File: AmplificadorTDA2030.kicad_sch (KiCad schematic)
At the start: 36 parts, among them J1 SJ1-3523N, J2 DC-005, J3 Speaker, U1 TDA2030, U2 TDA2030

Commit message: Librerias de Simbolos,Footprints y Modelos 3D Agregados
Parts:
- J2: footprint Footprints y Simbolos:NINIGI_DC-005 -> DC-005 - Connector Alimentacion:NINIGI_DC-005
- RV1: footprint Connector_PinSocket_2.00mm:PinSocket_2x03_P2.00mm_Vertical -> Potentiometer_THT:Potentiometer_Alps_RK163_Dual_Horizontal
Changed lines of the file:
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@@
 			)
 		)
-		(property "Footprint" "Connector_PinSocket_2.00mm:PinSocket_2x03_P2.00mm_Vertical"
+		(property "Footprint" "Potentiometer_THT:Potentiometer_Alps_RK163_Dual_Horizontal"
 			(at 118.745 86.36 0)
 			(effects
@@
 			)
 		)
-		(property "Footprint" "Footprints y Simbolos:NINIGI_DC-005"
+		(property "Footprint" "DC-005 - Connector Alimentacion:NINIGI_DC-005"
 			(at 91.44 38.1 0)
 			(effects

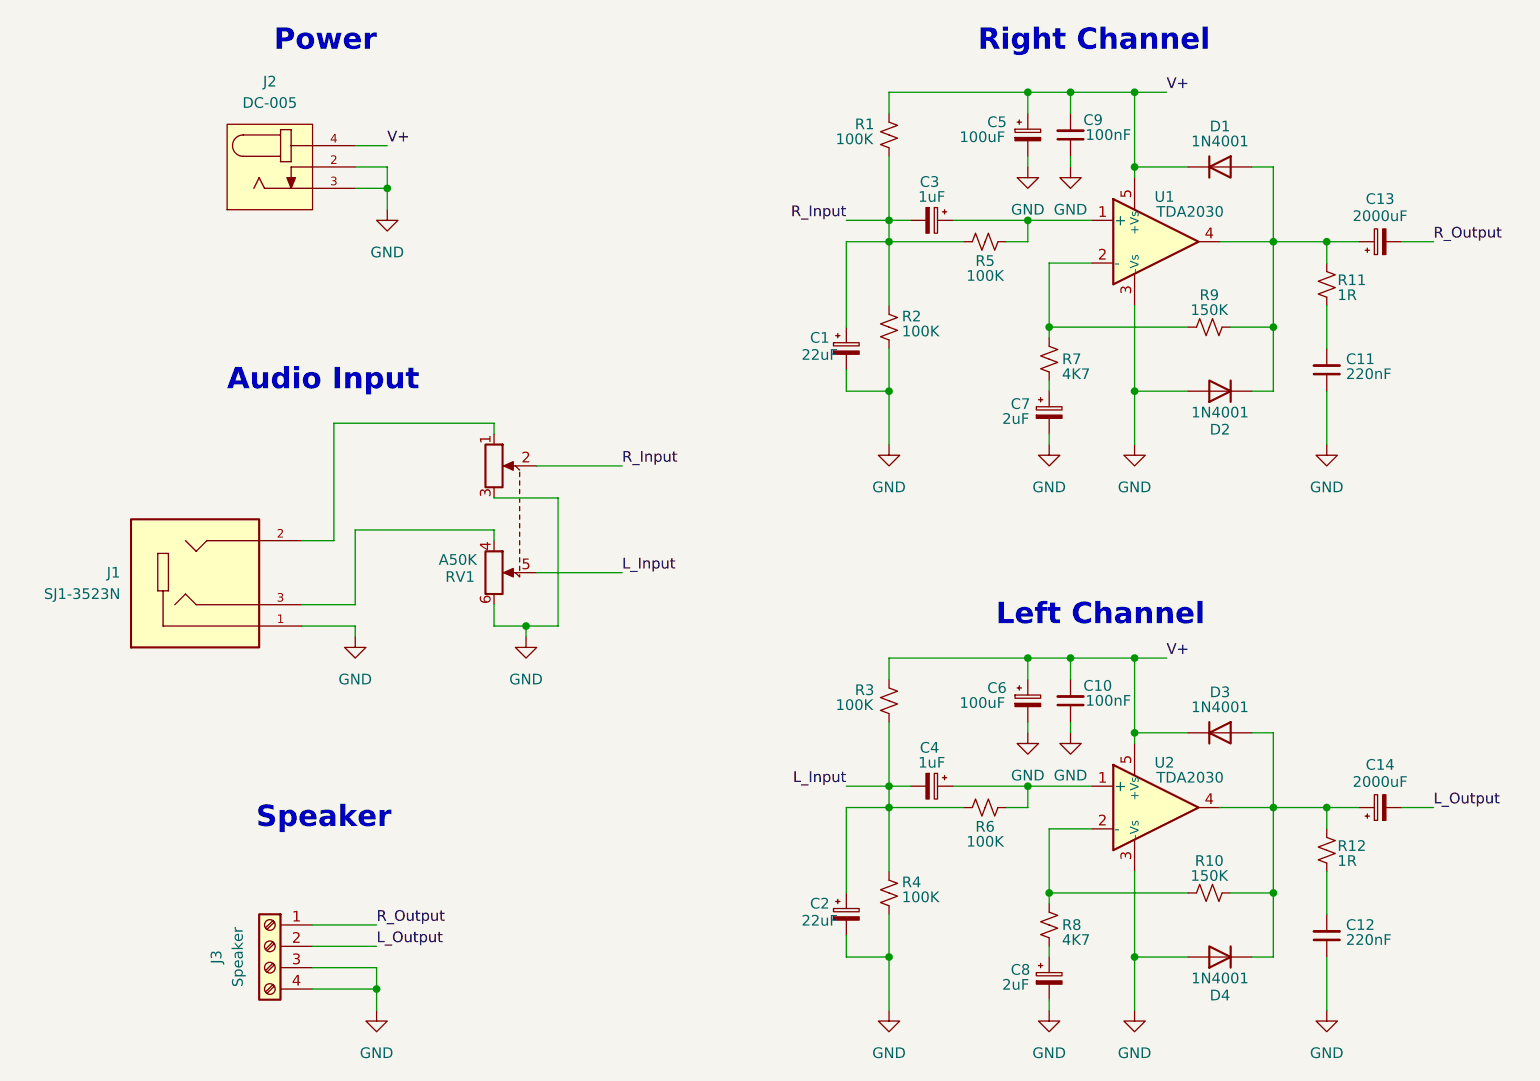
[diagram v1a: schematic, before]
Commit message: Footprints Asignados
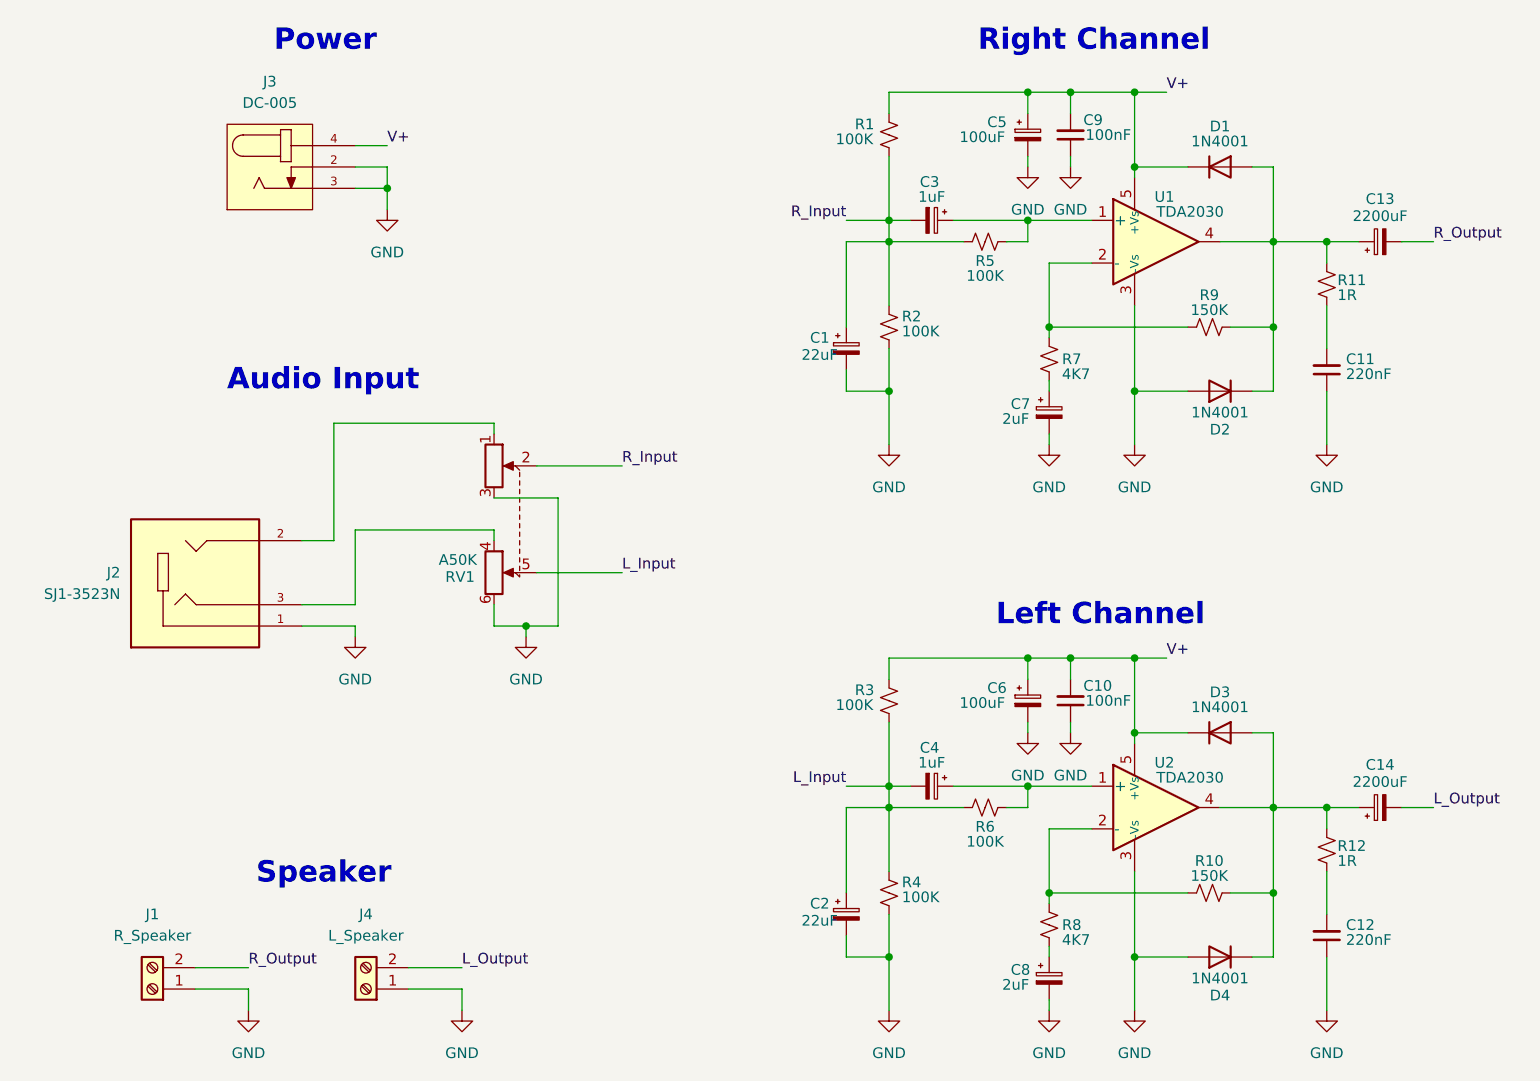
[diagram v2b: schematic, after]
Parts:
- removed J3: Speaker, Connector:FanPinHeader_1x04_P2.54mm_Vertical, symbol Connector:Screw_Terminal_01x04
- added J1: R_Speaker, TerminalBlock_Phoenix:TerminalBlock_Phoenix_MKDS-1,5-2-5.08_1x02_P5.08mm_Horizontal, symbol Connector:Screw_Terminal_01x02
- added J4: L_Speaker, TerminalBlock_Phoenix:TerminalBlock_Phoenix_MKDS-1,5-2-5.08_1x02_P5.08mm_Horizontal, symbol Connector:Screw_Terminal_01x02
- C1, C2, C5, C6: footprint Capacitor_THT:CP_Radial_D10.0mm_P5.00mm -> Capacitor_THT:CP_Radial_D6.3mm_P2.50mm
- C10, C11, C12, C9: footprint Capacitor_THT:CP_Radial_D10.0mm_P5.00mm -> Capacitor_THT:C_Disc_D3.0mm_W2.0mm_P2.50mm
- C13, C14: value 2000uF -> 2200uF; footprint Capacitor_THT:CP_Radial_D10.0mm_P5.00mm -> Capacitor_THT:CP_Radial_D16.0mm_P7.50mm
- C3, C4, C7, C8: footprint Capacitor_THT:CP_Radial_D10.0mm_P5.00mm -> Capacitor_THT:CP_Radial_D4.0mm_P2.00mm
- renumbered J1 to J2, J2 to J3
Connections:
- net GND: now also J1.1 (Pin_1), J4.1 (Pin_1)
- net L_Output: now also J4.2 (Pin_2)
- net R_Output: now also J1.2 (Pin_2)

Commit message: Ruteo de PCB correcto
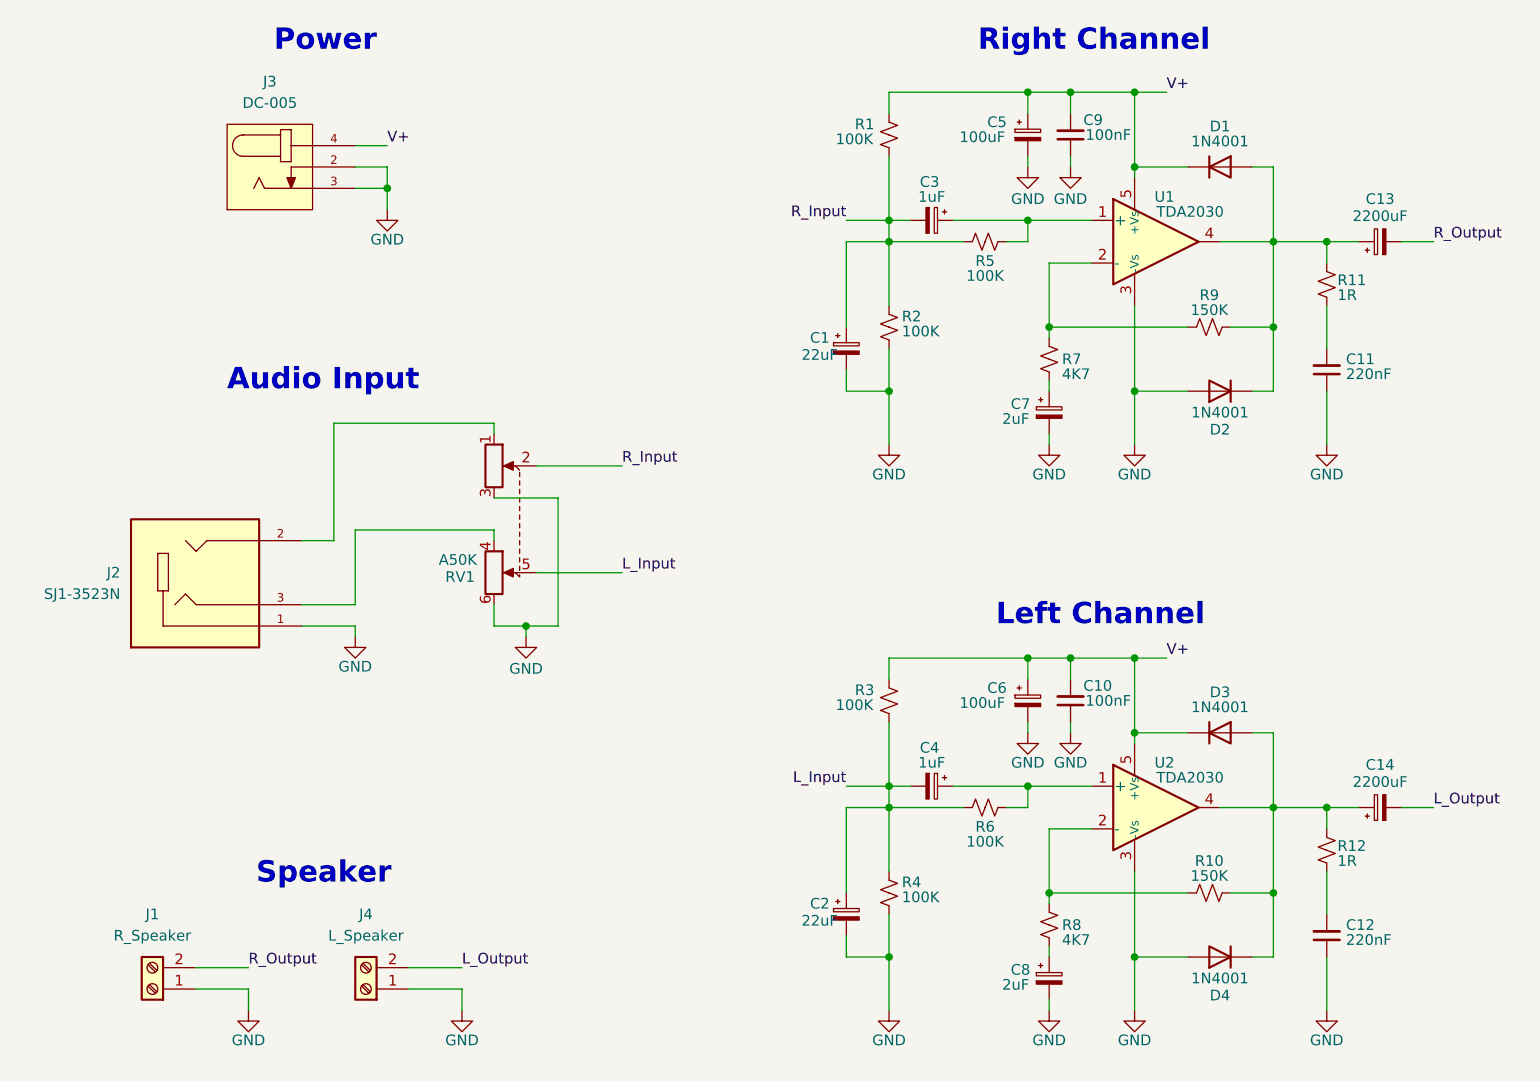
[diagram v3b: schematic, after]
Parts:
- R10, R11, R12, R7, R9: footprint Resistor_THT:R_Axial_DIN0204_L3.6mm_D1.6mm_P5.08mm_Horizontal -> Resistor_THT:R_Axial_DIN0204_L3.6mm_D1.6mm_P7.62mm_Horizontal
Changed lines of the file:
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@@
 			)
 		)
-		(property "Footprint" "Resistor_THT:R_Axial_DIN0204_L3.6mm_D1.6mm_P5.08mm_Horizontal"
+		(property "Footprint" "Resistor_THT:R_Axial_DIN0204_L3.6mm_D1.6mm_P7.62mm_Horizontal"
 			(at 203.2 57.15 0)
 			(effects
@@
 		(on_board yes)
 		(dnp no)
-		(fields_autoplaced yes)
 		(property "Reference" "#PWR06"
 			(at 165.1 77.47 0)
@@
 		)
 		(property "Value" "GND"
-			(at 165.1 76.2 0)
+			(at 165.1 74.676 0)
 			(effects
 				(font
@@
 		(on_board yes)
 		(dnp no)
-		(fields_autoplaced yes)
 		(property "Reference" "#PWR010"
 			(at 184.15 77.47 0)
@@
 		)
 		(property "Value" "GND"
-			(at 184.15 76.2 0)
+			(at 184.15 74.676 0)
 			(effects
 				(font
@@
 		(on_board yes)
 		(dnp no)
-		(fields_autoplaced yes)
 		(property "Reference" "#PWR09"
 			(at 181.61 111.76 0)
@@
 		)
 		(property "Value" "GND"
-			(at 181.61 110.49 0)
+			(at 181.61 108.966 0)
 			(effects
 				(font
@@
 		(on_board yes)
 		(dnp no)
-		(fields_autoplaced yes)
 		(property "Reference" "#PWR07"
 			(at 165.1 144.78 0)
@@
 		)
 		(property "Value" "GND"
-			(at 165.1 143.51 0)
+			(at 165.1 141.986 0)
 			(effects
 				(font
@@
 		(on_board yes)
 		(dnp no)
-		(fields_autoplaced yes)
 		(property "Reference" "#PWR017"
 			(at 217.17 144.78 0)
@@
 		)
 		(property "Value" "GND"
-			(at 217.17 143.51 0)
+			(at 217.17 141.986 0)
 			(effects
 				(font
@@
 		(on_board yes)
 		(dnp no)
-		(fields_autoplaced yes)
 		(property "Reference" "#PWR03"
 			(at 105.41 49.53 0)
@@
 		)
 		(property "Value" "GND"
-			(at 105.41 48.26 0)
+			(at 105.41 46.736 0)
 			(effects
 				(font
@@
 		(on_board yes)
 		(dnp no)
-		(fields_autoplaced yes)
 		(property "Reference" "#PWR013"
 			(at 186.69 111.76 0)
@@
 		)
 		(property "Value" "GND"
-			(at 186.69 110.49 0)
+			(at 186.69 108.966 0)
 			(effects
 				(font
@@
 			)
 		)
-		(property "Footprint" "Resistor_THT:R_Axial_DIN0204_L3.6mm_D1.6mm_P5.08mm_Horizontal"
+		(property "Footprint" "Resistor_THT:R_Axial_DIN0204_L3.6mm_D1.6mm_P7.62mm_Horizontal"
 			(at 184.15 60.96 0)
 			(effects
@@
 		(on_board yes)
 		(dnp no)
-		(fields_autoplaced yes)
 		(property "Reference" "#PWR015"
 			(at 194.31 144.78 0)
@@
 		)
 		(property "Value" "GND"
-			(at 194.31 143.51 0)
+			(at 194.31 141.986 0)
 			(effects
 				(font
@@
 		(on_board yes)
 		(dnp no)
-		(fields_autoplaced yes)
 		(property "Reference" "#PWR016"
 			(at 217.17 77.47 0)
@@
 		)
 		(property "Value" "GND"
-			(at 217.17 76.2 0)
+			(at 217.17 74.676 0)
 			(effects
 				(font
@@
 		(on_board yes)
 		(dnp no)
-		(fields_autoplaced yes)
 		(property "Reference" "#PWR014"
 			(at 194.31 77.47 0)
@@
 		)
 		(property "Value" "GND"
-			(at 194.31 76.2 0)
+			(at 194.31 74.676 0)
 			(effects
 				(font
@@
 			)
 		)
-		(property "Footprint" "Resistor_THT:R_Axial_DIN0204_L3.6mm_D1.6mm_P5.08mm_Horizontal"
+		(property "Footprint" "Resistor_THT:R_Axial_DIN0204_L3.6mm_D1.6mm_P7.62mm_Horizontal"
 			(at 217.17 119.38 0)
 			(effects
@@
 		(on_board yes)
 		(dnp no)
-		(fields_autoplaced yes)
 		(property "Reference" "#PWR02"
 			(at 101.6 100.33 0)
@@
 		)
 		(property "Value" "GND"
-			(at 101.6 99.06 0)
+			(at 101.6 97.536 0)
 			(effects
 				(font
@@
 			)
 		)
-		(property "Footprint" "Resistor_THT:R_Axial_DIN0204_L3.6mm_D1.6mm_P5.08mm_Horizontal"
+		(property "Footprint" "Resistor_THT:R_Axial_DIN0204_L3.6mm_D1.6mm_P7.62mm_Horizontal"
 			(at 217.17 52.07 0)
 			(effects
@@
 		(on_board yes)
 		(dnp no)
-		(fields_autoplaced yes)
 		(property "Reference" "#PWR012"
 			(at 186.69 44.45 0)
@@
 		)
 		(property "Value" "GND"
-			(at 186.69 43.18 0)
+			(at 186.69 41.91 0)
 			(effects
 				(font
@@
 		(on_board yes)
 		(dnp no)
-		(fields_autoplaced yes)
 		(property "Reference" "#PWR04"
 			(at 114.3 144.78 0)
@@
 		)
 		(property "Value" "GND"
-			(at 114.3 143.51 0)
+			(at 114.3 141.986 0)
 			(effects
 				(font
@@
 		(on_board yes)
 		(dnp no)
-		(fields_autoplaced yes)
 		(property "Reference" "#PWR08"
 			(at 181.61 44.45 0)
@@
 		)
 		(property "Value" "GND"
-			(at 181.61 43.18 0)
+			(at 181.61 41.91 0)
 			(effects
 				(font
@@
 		)
 		(property "Value" "GND"
-			(at 88.9 143.51 0)
+			(at 88.9 141.986 0)
 			(effects
 				(font
@@
 		(on_board yes)
 		(dnp no)
-		(fields_autoplaced yes)
 		(property "Reference" "#PWR05"
 			(at 121.92 100.33 0)
@@
 		)
 		(property "Value" "GND"
-			(at 121.92 99.06 0)
+			(at 121.92 97.79 0)
 			(effects
 				(font
@@
 		(on_board yes)
 		(dnp no)
-		(fields_autoplaced yes)
 		(property "Reference" "#PWR011"
 			(at 184.15 144.78 0)
@@
 		)
 		(property "Value" "GND"
-			(at 184.15 143.51 0)
+			(at 184.15 141.986 0)
 			(effects
 				(font
@@
 			)
 		)
-		(property "Footprint" "Resistor_THT:R_Axial_DIN0204_L3.6mm_D1.6mm_P5.08mm_Horizontal"
+		(property "Footprint" "Resistor_THT:R_Axial_DIN0204_L3.6mm_D1.6mm_P7.62mm_Horizontal"
 			(at 203.2 124.46 0)
 			(effects

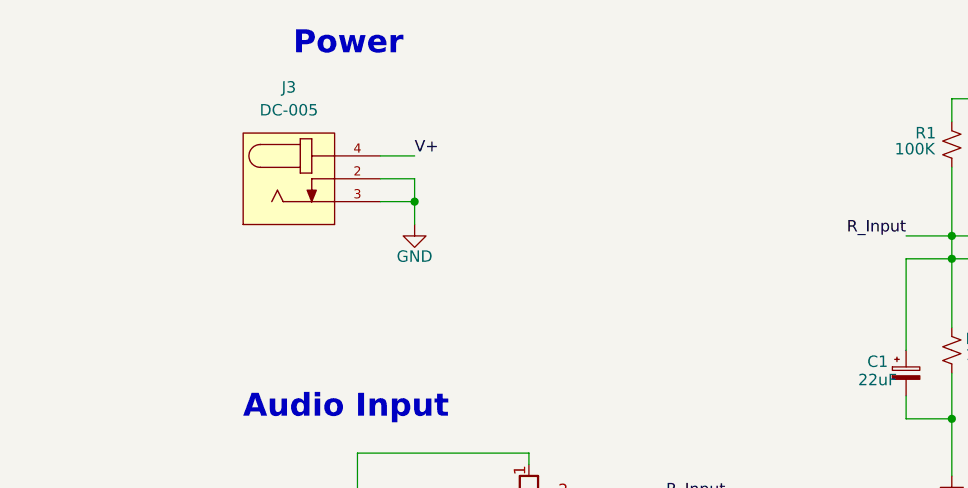
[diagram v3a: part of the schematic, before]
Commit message: Se agrega LED y Disipadores
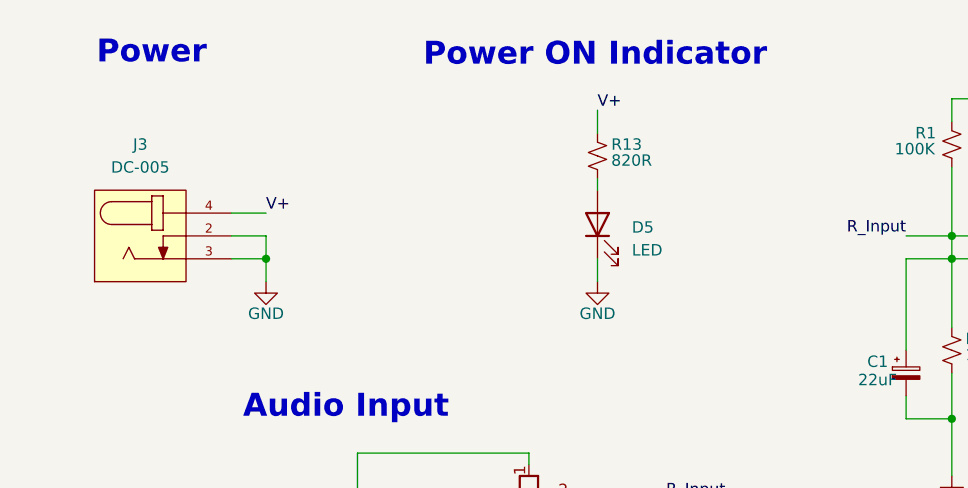
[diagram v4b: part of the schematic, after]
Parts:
- added D5: LED, LED_THT:LED_D5.0mm, symbol Device:LED
- added R13: 820R, Resistor_THT:R_Axial_DIN0204_L3.6mm_D1.6mm_P7.62mm_Horizontal, symbol Device:R_Small_US
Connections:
- net GND: now also D5.1 (K)
- net V+: now also R13.2
- new net: D5.2 (A), R13.1
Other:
- note added: "Power ON Indicator"
- moved on the sheet: J3
